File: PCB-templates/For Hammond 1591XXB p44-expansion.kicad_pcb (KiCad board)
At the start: 2 copper layers, 108 x 56 mm, 2 parts

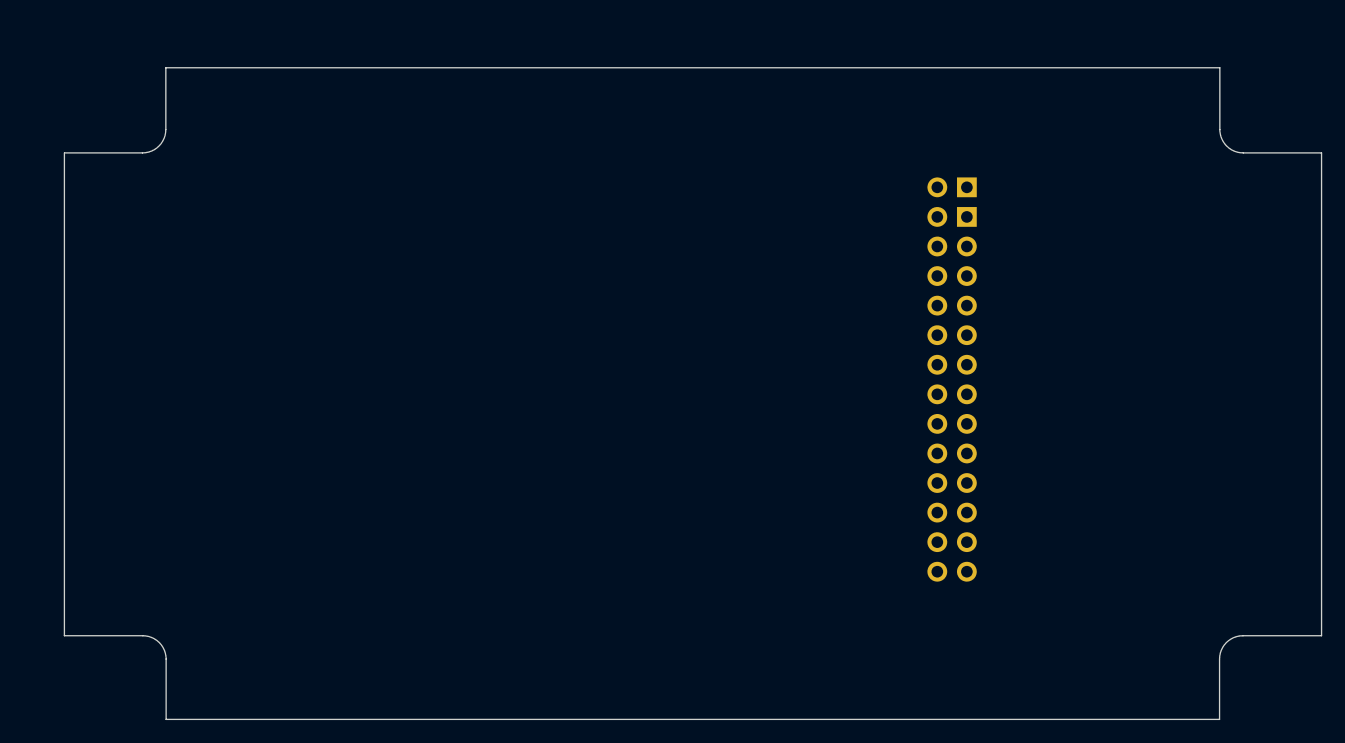
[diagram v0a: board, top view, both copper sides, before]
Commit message: Templates for Hammond 1591XXB redrawn, higher precision
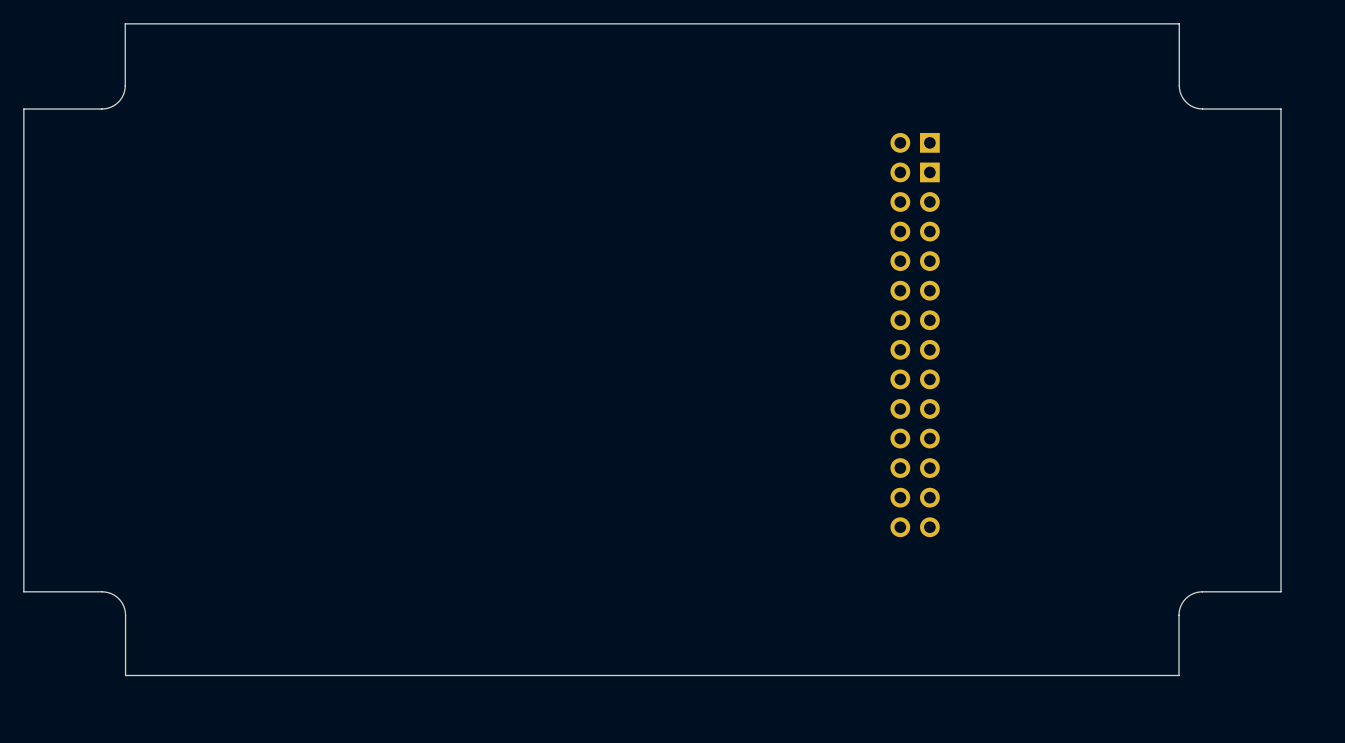
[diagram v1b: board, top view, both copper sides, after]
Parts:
- REF**: value P44-extra-pins -> P44-Extra
- REF**: value P44-extension -> P44-Expansion
- moved REF** 4.97 mm to (137.6, 73.0)
- moved REF** 4.97 mm to (137.6, 70.5)

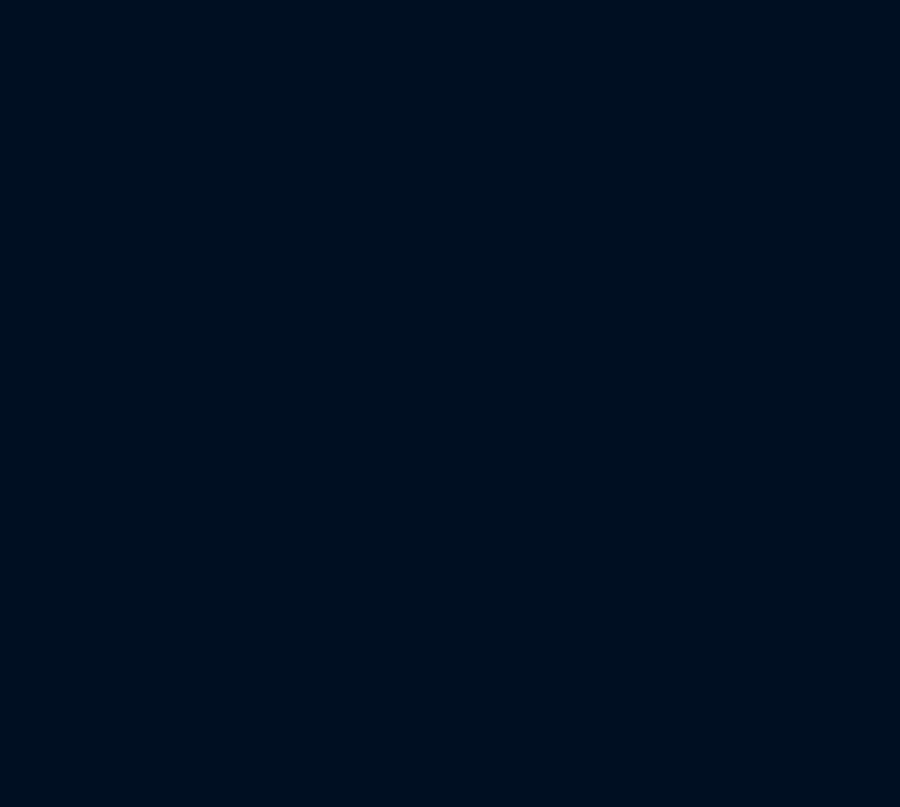
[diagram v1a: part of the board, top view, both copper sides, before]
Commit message: pp4-expansion: add minimized version of expansion header when pcb is mainboard
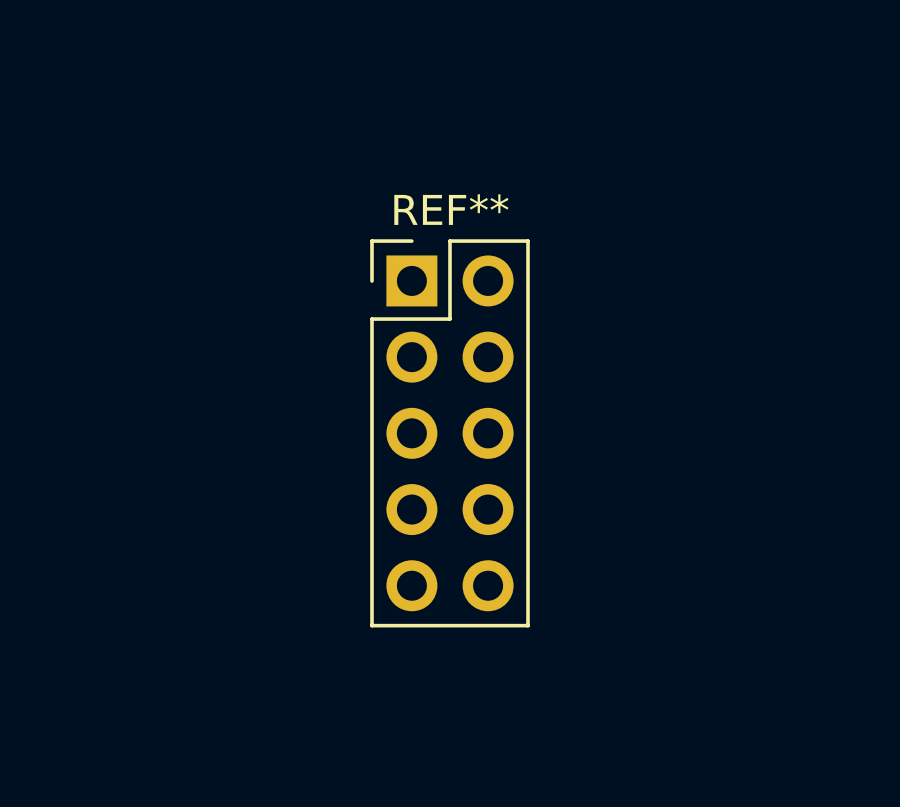
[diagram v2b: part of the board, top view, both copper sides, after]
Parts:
- added REF**: PinHeader_2x05_P2.54mm_Vertical, Connector_PinHeader_2.54mm:PinHeader_2x05_P2.54mm_Vertical, F.Cu at (89.9, 73.0)
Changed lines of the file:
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@@
   (general
     (thickness 1.6)
-    (drawings 217)
+    (drawings 221)
     (tracks 0)
     (zones 0)
-    (modules 2)
+    (modules 3)
     (nets 1)
   )
@@
     (uvia_drill 0.1)
   )
+  (module Connector_PinHeader_2.54mm:PinHeader_2x05_P2.54mm_Vertical locked (layer F.Cu)
+    (at 89.92 73)
+    (descr "Through hole straight pin header, 2x05, 2.54mm pitch, double rows")
+    (tags "Through hole pin header THT 2x05 2.54mm double row")
+    (fp_text reference REF** (at 1.27 -2.33) (layer F.SilkS)
+      (effects (font (size 1 1) (thickness 0.15)))
+    )
+    (fp_text value PinHeader_2x05_P2.54mm_Vertical (at 1.27 12.49) (layer F.Fab) hide
+      (effects (font (size 1 1) (thickness 0.15)))
+    )
+    (fp_text user %R (at 1.27 5.08 90) (layer F.Fab)
+      (effects (font (size 1 1) (thickness 0.15)))
+    )
+    (fp_line (start 4.35 -1.8) (end -1.8 -1.8) (layer F.CrtYd) (width 0.05))
+    (fp_line (start 4.35 11.95) (end 4.35 -1.8) (layer F.CrtYd) (width 0.05))
+    (fp_line (start -1.8 11.95) (end 4.35 11.95) (layer F.CrtYd) (width 0.05))
+    (fp_line (start -1.8 -1.8) (end -1.8 11.95) (layer F.CrtYd) (width 0.05))
+    (fp_line (start -1.33 -1.33) (end 0 -1.33) (layer F.SilkS) (width 0.12))
+    (fp_line (start -1.33 0) (end -1.33 -1.33) (layer F.SilkS) (width 0.12))
+    (fp_line (start 1.27 -1.33) (end 3.87 -1.33) (layer F.SilkS) (width 0.12))
+    (fp_line (start 1.27 1.27) (end 1.27 -1.33) (layer F.SilkS) (width 0.12))
+    (fp_line (start -1.33 1.27) (end 1.27 1.27) (layer F.SilkS) (width 0.12))
+    (fp_line (start 3.87 -1.33) (end 3.87 11.49) (layer F.SilkS) (width 0.12))
+    (fp_line (start -1.33 1.27) (end -1.33 11.49) (layer F.SilkS) (width 0.12))
+    (fp_line (start -1.33 11.49) (end 3.87 11.49) (layer F.SilkS) (width 0.12))
+    (fp_line (start -1.27 0) (end 0 -1.27) (layer F.Fab) (width 0.1))
+    (fp_line (start -1.27 11.43) (end -1.27 0) (layer F.Fab) (width 0.1))
+    (fp_line (start 3.81 11.43) (end -1.27 11.43) (layer F.Fab) (width 0.1))
+    (fp_line (start 3.81 -1.27) (end 3.81 11.43) (layer F.Fab) (width 0.1))
+    (fp_line (start 0 -1.27) (end 3.81 -1.27) (layer F.Fab) (width 0.1))
+    (pad 10 thru_hole oval (at 2.54 10.16) (size 1.7 1.7) (drill 1) (layers *.Cu *.Mask))
+    (pad 9 thru_hole oval (at 0 10.16) (size 1.7 1.7) (drill 1) (layers *.Cu *.Mask))
+    (pad 8 thru_hole oval (at 2.54 7.62) (size 1.7 1.7) (drill 1) (layers *.Cu *.Mask))
+    (pad 7 thru_hole oval (at 0 7.62) (size 1.7 1.7) (drill 1) (layers *.Cu *.Mask))
+    (pad 6 thru_hole oval (at 2.54 5.08) (size 1.7 1.7) (drill 1) (layers *.Cu *.Mask))
+    (pad 5 thru_hole oval (at 0 5.08) (size 1.7 1.7) (drill 1) (layers *.Cu *.Mask))
+    (pad 4 thru_hole oval (at 2.54 2.54) (size 1.7 1.7) (drill 1) (layers *.Cu *.Mask))
+    (pad 3 thru_hole oval (at 0 2.54) (size 1.7 1.7) (drill 1) (layers *.Cu *.Mask))
+    (pad 2 thru_hole oval (at 2.54 0) (size 1.7 1.7) (drill 1) (layers *.Cu *.Mask))
+    (pad 1 thru_hole rect (at 0 0) (size 1.7 1.7) (drill 1) (layers *.Cu *.Mask))
+    (model ${KISYS3DMOD}/Connector_PinHeader_2.54mm.3dshapes/PinHeader_2x05_P2.54mm_Vertical.wrl
+      (at (xyz 0 0 0))
+      (scale (xyz 1 1 1))
+      (rotate (xyz 0 0 0))
+    )
+  )
   (module Connector_PinHeader_2.54mm:PinHeader_1x02_P2.54mm_Vertical (layer B.Cu)
     (at 137.6 70.46 90)
@@
     )
   )
-  (module Connector_PinHeader_2.54mm:PinHeader_2x13_P2.54mm_Vertical (layer B.Cu)
+  (module Connector_PinHeader_2.54mm:PinHeader_2x13_P2.54mm_Vertical locked (layer B.Cu)
     (at 137.6 73 180)
     (descr "Through hole straight pin header, 2x13, 2.54mm pitch, double rows")
@@
     )
   )
+  (gr_line (start 88.09 84.94) (end 94.28 84.95) (layer F.CrtYd) (width 0.05))
+  (gr_line (start 88.09 105.26) (end 88.09 84.94) (layer F.CrtYd) (width 0.05))
+  (gr_line (start 94.28 105.26) (end 88.09 105.26) (layer F.CrtYd) (width 0.05))
+  (gr_line (start 94.28 84.95) (end 94.28 105.26) (layer F.CrtYd) (width 0.05))
   (gr_circle (center 74.990931 69.99746) (end 76.790931 69.99746) (layer Dwgs.User) (width 0.15))
   (gr_circle (center 74.990931 69.99746) (end 78.790931 69.19746) (layer Dwgs.User) (width 0.15))
